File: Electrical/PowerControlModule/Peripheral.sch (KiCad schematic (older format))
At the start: 7 parts

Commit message: Adds new part library for SCR stuff. Gets buck converters and connectors to show up on PCB layout
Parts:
- removed BUCK_OUT_GND1, BUCK_OUT_VCC1, IN_GND_1, IN_VCC_1: Conn_01x01_Female, symbol Connector:Conn_01x01_Female
- added BUCK1: LM2596, SCR_KiCAD_Lib:LM2596, symbol SCR_KiCAD_Lib:LM2596
- CONN1: footprint (none) -> Connector_PinHeader_2.54mm:PinHeader_1x02_P2.54mm_Vertical
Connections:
- net GND_in: now also BUCK1.1 (IN-)
- net VCC_in: now also BUCK1.2 (IN+)
- net at PMOS1.2: now also BUCK1.4 (OUT+)
- net at CONN1.2 (Pin_2): now also BUCK1.3 (OUT-)
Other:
- moved on the sheet: CONN1, FUSE1, PMOS1
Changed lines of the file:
@@
 Comment4 ""
 $EndDescr
-$Comp
-L Connector:Conn_01x01_Female BUCK_OUT_VCC?
-U 1 1 5D952D31
-P 4900 2950
-AR Path="/5D952D31" Ref="BUCK_OUT_VCC?"  Part="1"
-AR Path="/5D94BB1B/5D952D31" Ref="BUCK_OUT_VCC1"  Part="1"
-AR Path="/5D97A274/5D952D31" Ref="BUCK_OUT_VCC2"  Part="1"
-AR Path="/5D98E0A5/5D952D31" Ref="BUCK_OUT_VCC3"  Part="1"
-AR Path="/5D98E0AC/5D952D31" Ref="BUCK_OUT_VCC4"  Part="1"
-AR Path="/5D992879/5D952D31" Ref="BUCK_OUT_VCC8"  Part="1"
-AR Path="/5D992880/5D952D31" Ref="BUCK_OUT_VCC7"  Part="1"
-AR Path="/5D99AFA5/5D952D31" Ref="BUCK_OUT_VCC5"  Part="1"
-AR Path="/5D99AFAC/5D952D31" Ref="BUCK_OUT_VCC6"  Part="1"
-F 0 "BUCK_OUT_VCC1" V 4838 2998 50  0000 L CNN
-F 1 "Conn_01x01_Female" V 4747 2998 50  0000 L CNN
-F 2 "" H 4900 2950 50  0001 C CNN
-F 3 "~" H 4900 2950 50  0001 C CNN
-	1    4900 2950
-	0    1    -1   0
-$EndComp
 Wire Wire Line
-	4900 3150 4900 3400
-$Comp
-L Connector:Conn_01x01_Female BUCK_OUT_GND?
-U 1 1 5D952D40
-P 4900 6000
-AR Path="/5D952D40" Ref="BUCK_OUT_GND?"  Part="1"
-AR Path="/5D94BB1B/5D952D40" Ref="BUCK_OUT_GND1"  Part="1"
-AR Path="/5D97A274/5D952D40" Ref="BUCK_OUT_GND2"  Part="1"
-AR Path="/5D98E0A5/5D952D40" Ref="BUCK_OUT_GND3"  Part="1"
-AR Path="/5D98E0AC/5D952D40" Ref="BUCK_OUT_GND4"  Part="1"
-AR Path="/5D992879/5D952D40" Ref="BUCK_OUT_GND8"  Part="1"
-AR Path="/5D992880/5D952D40" Ref="BUCK_OUT_GND7"  Part="1"
-AR Path="/5D99AFA5/5D952D40" Ref="BUCK_OUT_GND5"  Part="1"
-AR Path="/5D99AFAC/5D952D40" Ref="BUCK_OUT_GND6"  Part="1"
-F 0 "BUCK_OUT_GND1" V 4746 6048 50  0000 L CNN
-F 1 "Conn_01x01_Female" V 4837 6048 50  0000 L CNN
-F 2 "" H 4900 6000 50  0001 C CNN
-F 3 "~" H 4900 6000 50  0001 C CNN
-	1    4900 6000
-	0    1    1    0
-$EndComp
-$Comp
-L Connector:Conn_01x01_Female IN_VCC_?
-U 1 1 5D952D46
-P 4900 2100
-AR Path="/5D952D46" Ref="IN_VCC_?"  Part="1"
-AR Path="/5D94BB1B/5D952D46" Ref="IN_VCC_1"  Part="1"
-AR Path="/5D97A274/5D952D46" Ref="IN_VCC_2"  Part="1"
-AR Path="/5D98E0A5/5D952D46" Ref="IN_VCC_3"  Part="1"
-AR Path="/5D98E0AC/5D952D46" Ref="IN_VCC_4"  Part="1"
-AR Path="/5D992879/5D952D46" Ref="IN_VCC_8"  Part="1"
-AR Path="/5D992880/5D952D46" Ref="IN_VCC_7"  Part="1"
-AR Path="/5D99AFA5/5D952D46" Ref="IN_VCC_5"  Part="1"
-AR Path="/5D99AFAC/5D952D46" Ref="IN_VCC_6"  Part="1"
-F 0 "IN_VCC_1" V 4750 1700 50  0000 L CNN
-F 1 "Conn_01x01_Female" V 4850 1300 50  0000 L CNN
-F 2 "" H 4900 2100 50  0001 C CNN
-F 3 "~" H 4900 2100 50  0001 C CNN
-	1    4900 2100
-	0    -1   1    0
-$EndComp
-$Comp
-L Connector:Conn_01x01_Female IN_GND_?
-U 1 1 5D952D4C
-P 4900 2200
-AR Path="/5D952D4C" Ref="IN_GND_?"  Part="1"
-AR Path="/5D94BB1B/5D952D4C" Ref="IN_GND_1"  Part="1"
-AR Path="/5D97A274/5D952D4C" Ref="IN_GND_2"  Part="1"
-AR Path="/5D98E0A5/5D952D4C" Ref="IN_GND_3"  Part="1"
-AR Path="/5D98E0AC/5D952D4C" Ref="IN_GND_4"  Part="1"
-AR Path="/5D992879/5D952D4C" Ref="IN_GND_8"  Part="1"
-AR Path="/5D992880/5D952D4C" Ref="IN_GND_7"  Part="1"
-AR Path="/5D99AFA5/5D952D4C" Ref="IN_GND_5"  Part="1"
-AR Path="/5D99AFAC/5D952D4C" Ref="IN_GND_6"  Part="1"
-F 0 "IN_GND_1" V 4850 2600 50  0000 R CNN
-F 1 "Conn_01x01_Female" V 4750 3000 50  0000 R CNN
-F 2 "" H 4900 2200 50  0001 C CNN
-F 3 "~" H 4900 2200 50  0001 C CNN
-	1    4900 2200
-	0    1    -1   0
-$EndComp
+	6250 2300 6250 2550
 Wire Wire Line
-	4900 4200 4900 4000
+	6250 3350 6250 3150
 Wire Wire Line
-	4900 5250 4900 5000
+	6250 4400 6250 4150
 $Comp
 L LibraryLoader:64600001003 FUSE?
 U 1 1 5D952D5A
-P 4900 4200
+P 6250 3350
 AR Path="/5D952D5A" Ref="FUSE?"  Part="1"
 AR Path="/5D94BB1B/5D952D5A" Ref="FUSE1"  Part="1"
@@
 AR Path="/5D99AFA5/5D952D5A" Ref="FUSE5"  Part="1"
 AR Path="/5D99AFAC/5D952D5A" Ref="FUSE6"  Part="1"
-F 0 "FUSE1" H 5300 4465 50  0000 C CNN
-F 1 "64600001003" H 5300 4374 50  0000 C CNN
-F 2 "LibraryLoader:646-SERIESHOLDER" H 5550 4300 50  0001 L CNN
-F 3 "https://componentsearchengine.com/Datasheets/1/64600001003.pdf" H 5550 4200 50  0001 L CNN
-F 4 "Fuse Holder 5X20MM PC MNT" H 5550 4100 50  0001 L CNN "Description"
-F 5 "" H 5550 4000 50  0001 L CNN "Height"
-F 6 "576-64600001003" H 5550 3900 50  0001 L CNN "Mouser Part Number"
-F 7 "https://www.mouser.com/Search/Refine.aspx?Keyword=576-64600001003" H 5550 3800 50  0001 L CNN "Mouser Price/Stock"
-F 8 "LITTELFUSE" H 5550 3700 50  0001 L CNN "Manufacturer_Name"
-F 9 "64600001003" H 5550 3600 50  0001 L CNN "Manufacturer_Part_Number"
-	1    4900 4200
+F 0 "FUSE1" H 6650 3615 50  0000 C CNN
+F 1 "64600001003" H 6650 3524 50  0000 C CNN
+F 2 "LibraryLoader:646-SERIESHOLDER" H 6900 3450 50  0001 L CNN
+F 3 "https://componentsearchengine.com/Datasheets/1/64600001003.pdf" H 6900 3350 50  0001 L CNN
+F 4 "Fuse Holder 5X20MM PC MNT" H 6900 3250 50  0001 L CNN "Description"
+F 5 "" H 6900 3150 50  0001 L CNN "Height"
+F 6 "576-64600001003" H 6900 3050 50  0001 L CNN "Mouser Part Number"
+F 7 "https://www.mouser.com/Search/Refine.aspx?Keyword=576-64600001003" H 6900 2950 50  0001 L CNN "Mouser Price/Stock"
+F 8 "LITTELFUSE" H 6900 2850 50  0001 L CNN "Manufacturer_Name"
+F 9 "64600001003" H 6900 2750 50  0001 L CNN "Manufacturer_Part_Number"
+	1    6250 3350
 	0    1    1    0
 $EndComp
-Wire Wire Line
-	4900 5350 4900 5800
 $Comp
 L Connector_Generic:Conn_01x02 CONN?
 U 1 1 5D952D61
-P 5100 5250
+P 6450 4400
 AR Path="/5D952D61" Ref="CONN?"  Part="1"
 AR Path="/5D94BB1B/5D952D61" Ref="CONN1"  Part="1"
@@
 AR Path="/5D99AFA5/5D952D61" Ref="CONN5"  Part="1"
 AR Path="/5D99AFAC/5D952D61" Ref="CONN6"  Part="1"
-F 0 "CONN1" H 5180 5242 50  0000 L CNN
-F 1 "Conn_01x02" H 5180 5151 50  0000 L CNN
-F 2 "" H 5100 5250 50  0001 C CNN
-F 3 "~" H 5100 5250 50  0001 C CNN
-	1    5100 5250
+F 0 "CONN1" H 6530 4392 50  0000 L CNN
+F 1 "Conn_01x02" H 6530 4301 50  0000 L CNN
+F 2 "Connector_PinHeader_2.54mm:PinHeader_1x02_P2.54mm_Vertical" H 6450 4400 50  0001 C CNN
+F 3 "~" H 6450 4400 50  0001 C CNN
+	1    6450 4400
 	1    0    0    -1
 $EndComp
@@
 L LibraryLoader:IPP120P04P4L03AKSA1 PMOS?
 U 1 1 5D952D73
-P 4600 3800
+P 5950 2950
 AR Path="/5D952D73" Ref="PMOS?"  Part="1"
 AR Path="/5D94BB1B/5D952D73" Ref="PMOS1"  Part="1"
@@
 AR Path="/5D99AFA5/5D952D73" Ref="PMOS5"  Part="1"
 AR Path="/5D99AFAC/5D952D73" Ref="PMOS6"  Part="1"
-F 0 "PMOS1" H 5030 3946 50  0000 L CNN
-F 1 "IPP120P04P4L03AKSA1" H 5030 3855 50  0000 L CNN
-F 2 "LibraryLoader:TO254P440X1000X2110-3P" H 5050 3750 50  0001 L CNN
-F 3 "https://componentsearchengine.com/Datasheets/1/IPP120P04P4L03AKSA1.pdf" H 5050 3650 50  0001 L CNN
-F 4 "MOSFET P-Ch 40V 120A OptiMOS-P2 TO-220" H 5050 3550 50  0001 L CNN "Description"
-F 5 "4.4" H 5050 3450 50  0001 L CNN "Height"
-F 6 "726-IPP120P04P4L03AK" H 5050 3350 50  0001 L CNN "Mouser Part Number"
-F 7 "https://www.mouser.com/Search/Refine.aspx?Keyword=726-IPP120P04P4L03AK" H 5050 3250 50  0001 L CNN "Mouser Price/Stock"
-F 8 "Infineon" H 5050 3150 50  0001 L CNN "Manufacturer_Name"
-F 9 "IPP120P04P4L03AKSA1" H 5050 3050 50  0001 L CNN "Manufacturer_Part_Number"
-	1    4600 3800
+F 0 "PMOS1" H 6380 3096 50  0000 L CNN
+F 1 "IPP120P04P4L03AKSA1" H 6380 3005 50  0000 L CNN
+F 2 "LibraryLoader:TO254P440X1000X2110-3P" H 6400 2900 50  0001 L CNN
+F 3 "https://componentsearchengine.com/Datasheets/1/IPP120P04P4L03AKSA1.pdf" H 6400 2800 50  0001 L CNN
+F 4 "MOSFET P-Ch 40V 120A OptiMOS-P2 TO-220" H 6400 2700 50  0001 L CNN "Description"
+F 5 "4.4" H 6400 2600 50  0001 L CNN "Height"
+F 6 "726-IPP120P04P4L03AK" H 6400 2500 50  0001 L CNN "Mouser Part Number"
+F 7 "https://www.mouser.com/Search/Refine.aspx?Keyword=726-IPP120P04P4L03AK" H 6400 2400 50  0001 L CNN "Mouser Price/Stock"
+F 8 "Infineon" H 6400 2300 50  0001 L CNN "Manufacturer_Name"
+F 9 "IPP120P04P4L03AKSA1" H 6400 2200 50  0001 L CNN "Manufacturer_Part_Number"
+	1    5950 2950
 	1    0    0    -1
 $EndComp
-Text HLabel 4300 3800 0    50   Input ~ 0
+Text HLabel 5650 2950 0    50   Input ~ 0
 ENB
 Wire Wire Line
-	4300 3800 4600 3800
-Text HLabel 4500 2700 0    50   Input ~ 0
+	5650 2950 5950 2950
+Text HLabel 3950 3050 0    50   Input ~ 0
 GND_in
-Text HLabel 4500 1500 0    50   Input ~ 0
+Text HLabel 3900 2850 0    50   Input ~ 0
 VCC_in
 Wire Wire Line
-	4900 2700 4500 2700
+	4300 3050 3950 3050
 Wire Wire Line
-	4900 2400 4900 2700
+	3900 2850 4300 2850
+$Comp
+L SCR_KiCAD_Lib:LM2596 BUCK1
+U 1 1 5D897E7B
+P 4650 2600
+AR Path="/5D94BB1B/5D897E7B" Ref="BUCK1"  Part="1"
+AR Path="/5D97A274/5D897E7B" Ref="BUCK2"  Part="1"
+AR Path="/5D98E0A5/5D897E7B" Ref="BUCK3"  Part="1"
+AR Path="/5D98E0AC/5D897E7B" Ref="BUCK4"  Part="1"
+AR Path="/5D99AFA5/5D897E7B" Ref="BUCK5"  Part="1"
+AR Path="/5D99AFAC/5D897E7B" Ref="BUCK6"  Part="1"
+AR Path="/5D992880/5D897E7B" Ref="BUCK7"  Part="1"
+AR Path="/5D992879/5D897E7B" Ref="BUCK8"  Part="1"
+F 0 "BUCK1" H 4650 2615 50  0000 C CNN
+F 1 "LM2596" H 4650 2524 50  0000 C CNN
+F 2 "SCR_KiCAD_Lib:LM2596" H 4650 2600 50  0001 C CNN
+F 3 "" H 4650 2600 50  0001 C CNN
+	1    4650 2600
+	1    0    0    -1
+$EndComp
 Wire Wire Line
-	4500 1500 4900 1500
+	6250 4500 5250 4500
 Wire Wire Line
-	4900 1500 4900 1900
+	5250 4500 5250 3050
+Wire Wire Line
+	5250 3050 5000 3050
+Wire Wire Line
+	5000 2850 5250 2850
+Wire Wire Line
+	5250 2850 5250 2300
+Wire Wire Line
+	5250 2300 6250 2300
 $EndSCHEMATC

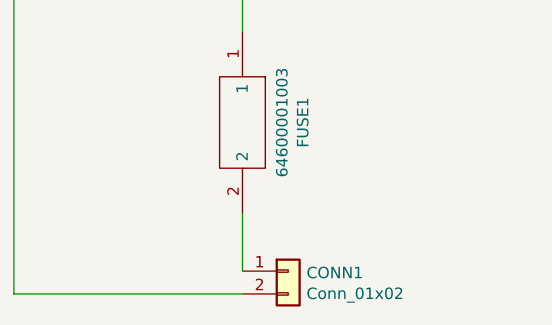
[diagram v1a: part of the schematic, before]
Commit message: Lays out power distribution board on PCB. Need to make 4 layer setup before routing. Also need to change motor output footprint
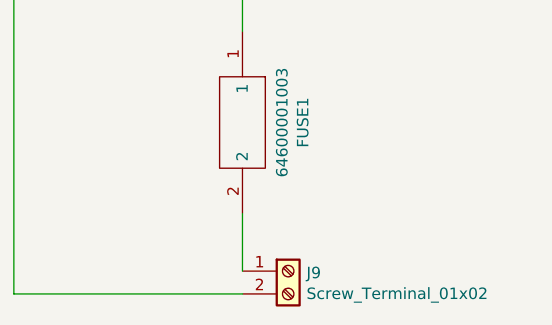
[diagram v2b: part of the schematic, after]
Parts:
- removed CONN1: Conn_01x02, Connector_PinHeader_2.54mm:PinHeader_1x02_P2.54mm_Vertical, symbol Connector_Generic:Conn_01x02
- added J9: Screw_Terminal_01x02, TerminalBlock_Phoenix:TerminalBlock_Phoenix_MKDS-3-2-5.08_1x02_P5.08mm_Horizontal, symbol Connector:Screw_Terminal_01x02
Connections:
- net at BUCK1.3 (OUT-): now also J9.2 (Pin_2)
- net at FUSE1.2: now also J9.1 (Pin_1)
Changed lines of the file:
@@
-$EndComp
-$Comp
-L Connector_Generic:Conn_01x02 CONN?
-U 1 1 5D952D61
-P 6450 4400
-AR Path="/5D952D61" Ref="CONN?"  Part="1"
-AR Path="/5D94BB1B/5D952D61" Ref="CONN1"  Part="1"
-AR Path="/5D97A274/5D952D61" Ref="CONN2"  Part="1"
-AR Path="/5D98E0A5/5D952D61" Ref="CONN3"  Part="1"
-AR Path="/5D98E0AC/5D952D61" Ref="CONN4"  Part="1"
-AR Path="/5D992879/5D952D61" Ref="CONN8"  Part="1"
-AR Path="/5D992880/5D952D61" Ref="CONN7"  Part="1"
-AR Path="/5D99AFA5/5D952D61" Ref="CONN5"  Part="1"
-AR Path="/5D99AFAC/5D952D61" Ref="CONN6"  Part="1"
-F 0 "CONN1" H 6530 4392 50  0000 L CNN
-F 1 "Conn_01x02" H 6530 4301 50  0000 L CNN
-F 2 "Connector_PinHeader_2.54mm:PinHeader_1x02_P2.54mm_Vertical" H 6450 4400 50  0001 C CNN
-F 3 "~" H 6450 4400 50  0001 C CNN
-	1    6450 4400
-	1    0    0    -1
 $EndComp
 $Comp
@@
 Wire Wire Line
 	5250 2300 6250 2300
+$Comp
+L Connector:Screw_Terminal_01x02 J9
+U 1 1 5D8A1568
+P 6450 4400
+AR Path="/5D94BB1B/5D8A1568" Ref="J9"  Part="1"
+AR Path="/5D97A274/5D8A1568" Ref="J10"  Part="1"
+AR Path="/5D98E0A5/5D8A1568" Ref="J11"  Part="1"
+AR Path="/5D98E0AC/5D8A1568" Ref="J12"  Part="1"
+AR Path="/5D99AFA5/5D8A1568" Ref="J13"  Part="1"
+AR Path="/5D99AFAC/5D8A1568" Ref="J14"  Part="1"
+AR Path="/5D992880/5D8A1568" Ref="J15"  Part="1"
+AR Path="/5D992879/5D8A1568" Ref="J16"  Part="1"
+F 0 "J9" H 6530 4392 50  0000 L CNN
+F 1 "Screw_Terminal_01x02" H 6530 4301 50  0000 L CNN
+F 2 "TerminalBlock_Phoenix:TerminalBlock_Phoenix_MKDS-3-2-5.08_1x02_P5.08mm_Horizontal" H 6450 4400 50  0001 C CNN
+F 3 "~" H 6450 4400 50  0001 C CNN
+	1    6450 4400
+	1    0    0    -1
+$EndComp
 $EndSCHEMATC

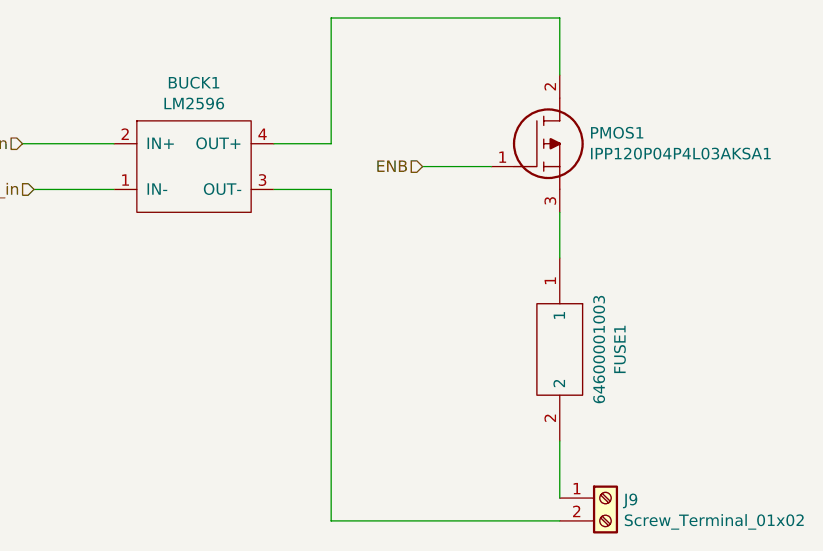
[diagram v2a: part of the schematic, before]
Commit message: Fixes silkscreen stuff and adds ground connection for motor control battery connection
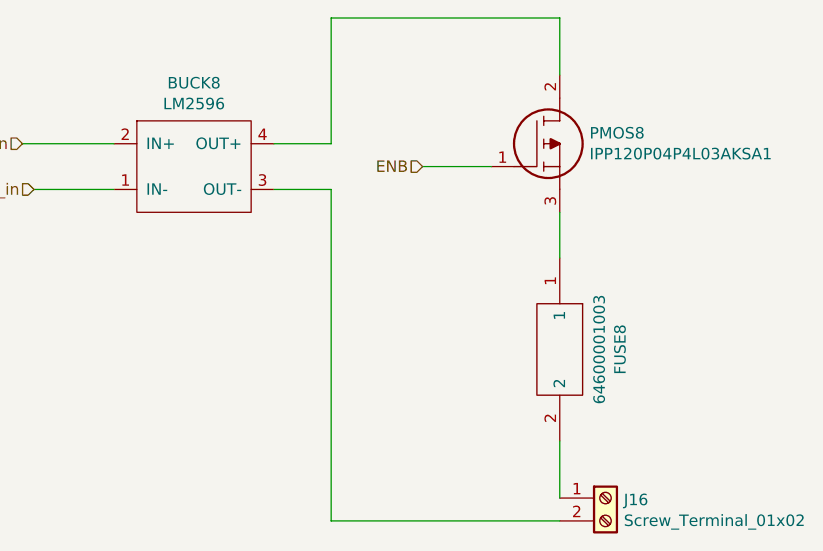
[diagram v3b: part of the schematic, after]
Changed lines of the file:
@@
 $Descr A4 11693 8268
 encoding utf-8
-Sheet 2 11
+Sheet 9 11
 Title ""
 Date ""
@@
 AR Path="/5D99AFA5/5D952D5A" Ref="FUSE5"  Part="1"
 AR Path="/5D99AFAC/5D952D5A" Ref="FUSE6"  Part="1"
-F 0 "FUSE1" H 6650 3615 50  0000 C CNN
+F 0 "FUSE8" H 6650 3615 50  0000 C CNN
 F 1 "64600001003" H 6650 3524 50  0000 C CNN
 F 2 "LibraryLoader:646-SERIESHOLDER" H 6900 3450 50  0001 L CNN
@@
 AR Path="/5D99AFA5/5D952D73" Ref="PMOS5"  Part="1"
 AR Path="/5D99AFAC/5D952D73" Ref="PMOS6"  Part="1"
-F 0 "PMOS1" H 6380 3096 50  0000 L CNN
+F 0 "PMOS8" H 6380 3096 50  0000 L CNN
 F 1 "IPP120P04P4L03AKSA1" H 6380 3005 50  0000 L CNN
 F 2 "LibraryLoader:TO254P440X1000X2110-3P" H 6400 2900 50  0001 L CNN
@@
 AR Path="/5D992880/5D897E7B" Ref="BUCK7"  Part="1"
 AR Path="/5D992879/5D897E7B" Ref="BUCK8"  Part="1"
-F 0 "BUCK1" H 4650 2615 50  0000 C CNN
+F 0 "BUCK8" H 4650 2615 50  0000 C CNN
 F 1 "LM2596" H 4650 2524 50  0000 C CNN
 F 2 "SCR_KiCAD_Lib:LM2596" H 4650 2600 50  0001 C CNN
@@
 AR Path="/5D992880/5D8A1568" Ref="J15"  Part="1"
 AR Path="/5D992879/5D8A1568" Ref="J16"  Part="1"
-F 0 "J9" H 6530 4392 50  0000 L CNN
+F 0 "J16" H 6530 4392 50  0000 L CNN
 F 1 "Screw_Terminal_01x02" H 6530 4301 50  0000 L CNN
 F 2 "TerminalBlock_Phoenix:TerminalBlock_Phoenix_MKDS-3-2-5.08_1x02_P5.08mm_Horizontal" H 6450 4400 50  0001 C CNN

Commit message: Power control module grounding and power plane fixes
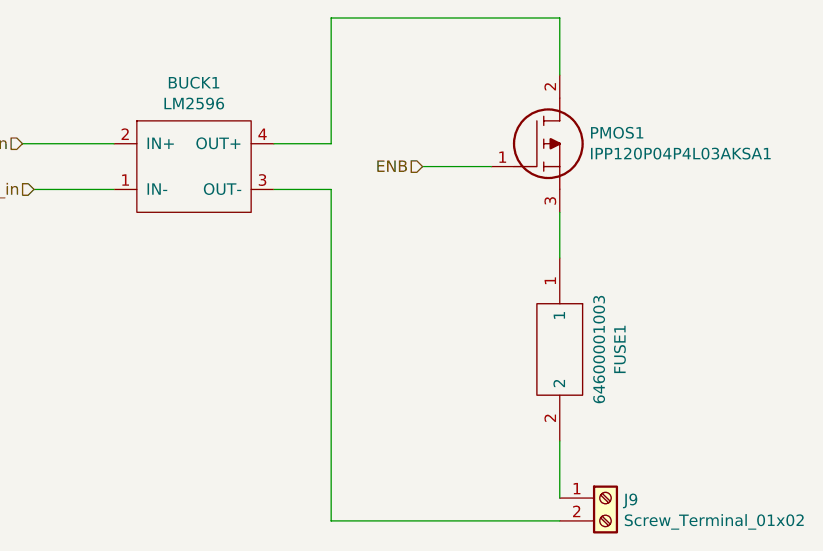
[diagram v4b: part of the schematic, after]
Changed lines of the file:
@@
 $Descr A4 11693 8268
 encoding utf-8
-Sheet 9 11
+Sheet 2 11
 Title ""
 Date ""
@@
 AR Path="/5D99AFA5/5D952D5A" Ref="FUSE5"  Part="1"
 AR Path="/5D99AFAC/5D952D5A" Ref="FUSE6"  Part="1"
-F 0 "FUSE8" H 6650 3615 50  0000 C CNN
+F 0 "FUSE1" H 6650 3615 50  0000 C CNN
 F 1 "64600001003" H 6650 3524 50  0000 C CNN
 F 2 "LibraryLoader:646-SERIESHOLDER" H 6900 3450 50  0001 L CNN
@@
 AR Path="/5D99AFA5/5D952D73" Ref="PMOS5"  Part="1"
 AR Path="/5D99AFAC/5D952D73" Ref="PMOS6"  Part="1"
-F 0 "PMOS8" H 6380 3096 50  0000 L CNN
+F 0 "PMOS1" H 6380 3096 50  0000 L CNN
 F 1 "IPP120P04P4L03AKSA1" H 6380 3005 50  0000 L CNN
 F 2 "LibraryLoader:TO254P440X1000X2110-3P" H 6400 2900 50  0001 L CNN
@@
 AR Path="/5D992880/5D897E7B" Ref="BUCK7"  Part="1"
 AR Path="/5D992879/5D897E7B" Ref="BUCK8"  Part="1"
-F 0 "BUCK8" H 4650 2615 50  0000 C CNN
+F 0 "BUCK1" H 4650 2615 50  0000 C CNN
 F 1 "LM2596" H 4650 2524 50  0000 C CNN
 F 2 "SCR_KiCAD_Lib:LM2596" H 4650 2600 50  0001 C CNN
@@
 AR Path="/5D992880/5D8A1568" Ref="J15"  Part="1"
 AR Path="/5D992879/5D8A1568" Ref="J16"  Part="1"
-F 0 "J16" H 6530 4392 50  0000 L CNN
+F 0 "J9" H 6530 4392 50  0000 L CNN
 F 1 "Screw_Terminal_01x02" H 6530 4301 50  0000 L CNN
 F 2 "TerminalBlock_Phoenix:TerminalBlock_Phoenix_MKDS-3-2-5.08_1x02_P5.08mm_Horizontal" H 6450 4400 50  0001 C CNN
